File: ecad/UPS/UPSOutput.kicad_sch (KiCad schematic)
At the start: 26 parts, among them J3 USB_C_Receptacle_USB2.0_16P, Q3 IRLR7843TRPBF, U2 MPQ5031GRE-0001-AEC1-P, U3 L78L05_SOT89

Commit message: Moved most components where they belong-ish
Barrel Jack's on the end as well as battery connector for now.  The MOSFET's need to be really close to the caps in the charger module
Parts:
- C10, C11, C12, C60: footprint Capacitor_SMD:C_0805_2012Metric_Pad1.18x1.45mm_HandSolder -> (none)
- C5, C59, C6, C7, C8, C9: footprint Capacitor_SMD:C_0603_1608Metric_Pad1.08x0.95mm_HandSolder -> (none)
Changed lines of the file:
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@@
 			)
 		)
-		(property "Footprint" "Capacitor_SMD:C_0603_1608Metric_Pad1.08x0.95mm_HandSolder"
+		(property "Footprint" ""
 			(at 204.1652 78.74 0)
 			(effects
@@
 			)
 		)
-		(property "Footprint" "Capacitor_SMD:C_0603_1608Metric_Pad1.08x0.95mm_HandSolder"
+		(property "Footprint" ""
 			(at 30.1752 115.57 0)
 			(effects
@@
 			)
 		)
-		(property "Footprint" "Capacitor_SMD:C_0603_1608Metric_Pad1.08x0.95mm_HandSolder"
+		(property "Footprint" ""
 			(at 65.7352 78.74 0)
 			(effects
@@
 			)
 		)
-		(property "Footprint" "Capacitor_SMD:C_0603_1608Metric_Pad1.08x0.95mm_HandSolder"
+		(property "Footprint" ""
 			(at 130.5052 73.66 0)
 			(effects
@@
 			)
 		)
-		(property "Footprint" "Capacitor_SMD:C_0805_2012Metric_Pad1.18x1.45mm_HandSolder"
+		(property "Footprint" ""
 			(at 56.1848 78.74 0)
 			(effects
@@
 			)
 		)
-		(property "Footprint" "Capacitor_SMD:C_0805_2012Metric_Pad1.18x1.45mm_HandSolder"
+		(property "Footprint" ""
 			(at 143.51 81.5848 0)
 			(effects
@@
 			)
 		)
-		(property "Footprint" "Capacitor_SMD:C_0603_1608Metric_Pad1.08x0.95mm_HandSolder"
+		(property "Footprint" ""
 			(at 135.5852 73.66 0)
 			(effects
@@
 			)
 		)
-		(property "Footprint" "Capacitor_SMD:C_0603_1608Metric_Pad1.08x0.95mm_HandSolder"
+		(property "Footprint" ""
 			(at 176.8348 78.74 0)
 			(effects
@@
 			)
 		)
-		(property "Footprint" "Capacitor_SMD:C_0805_2012Metric_Pad1.18x1.45mm_HandSolder"
+		(property "Footprint" ""
 			(at 30.1752 128.27 0)
 			(effects
@@
 			)
 		)
-		(property "Footprint" "Capacitor_SMD:C_0805_2012Metric_Pad1.18x1.45mm_HandSolder"
+		(property "Footprint" ""
 			(at 234.95 84.1248 0)
 			(effects

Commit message: Need to finish some traces, DRC warnings are keeping me from routing to the BQ,
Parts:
- added R35: 68.1k, Resistor_SMD:R_0805_2012Metric_Pad1.20x1.40mm_HandSolder, symbol Device:R
- added SW3: SW_DPDT_x2, UPS:SW_EG1218, symbol Switch:SW_DPDT_x2
- C10, C11, C12, C60: footprint (none) -> Capacitor_SMD:C_0805_2012Metric_Pad1.18x1.45mm_HandSolder
- C5, C59, C6, C7, C8, C9: footprint (none) -> Capacitor_SMD:C_0603_1608Metric_Pad1.08x0.95mm_HandSolder
- R6, R7: footprint (none) -> Resistor_SMD:R_1206_3216Metric_Pad1.30x1.75mm_HandSolder
- R8: footprint (none) -> Resistor_SMD:R_0805_2012Metric_Pad1.20x1.40mm_HandSolder
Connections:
- net GND: now also R35.2
- net D+: now reaches C7.1, D4.1 (K), J3.A6 (D+), J3.B6 (D+), U2.16 (DP)
- net CC1: now reaches D1.1 (K), J3.A5 (CC1), R7.1
- net VBUS_out: now reaches C11.2, C12.1, D5.1 (K), J3.A4 (VBUS), J3.A9 (VBUS), J3.B4 (VBUS), J3.B9 (VBUS), Q3.2 (D), TP6.1, U2.20 (VBUS_P)
- net D-: now reaches C8.1, D3.1 (K), J3.A7 (D-), J3.B7 (D-), U2.17 (DM)
- net CC2: now reaches D2.1 (K), J3.B5 (CC2), R6.2
- net at U2.19 (VDRV): now also SW3.1 (A); no longer Q3.1 (G)
- new net: Q3.1 (G), SW3.2 (B)
- new net: R35.1, SW3.3 (C)
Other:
- moved on the sheet: Q3

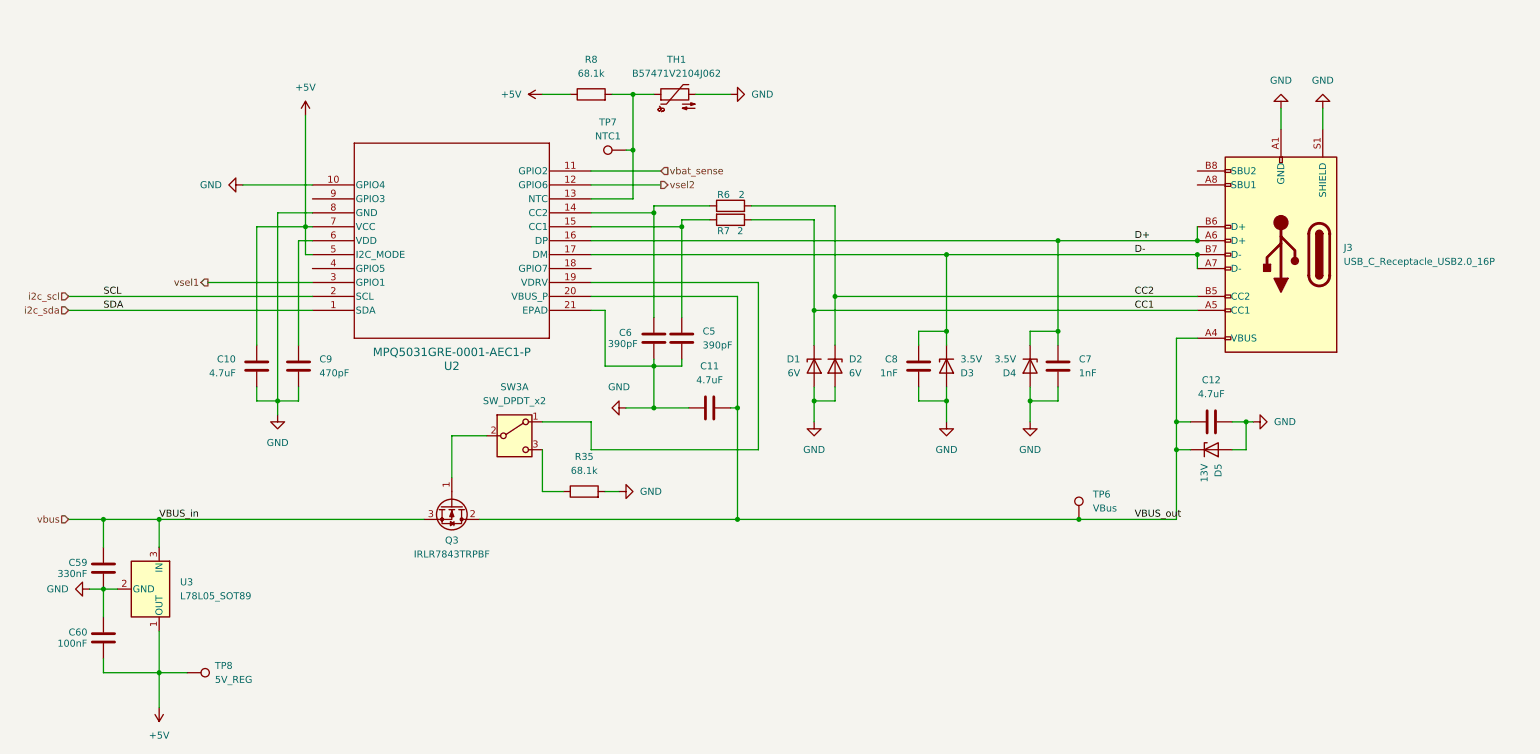
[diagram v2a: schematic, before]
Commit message: Ty's VBATSENSE Changes
Let me know if I messed this part up, did a small amount
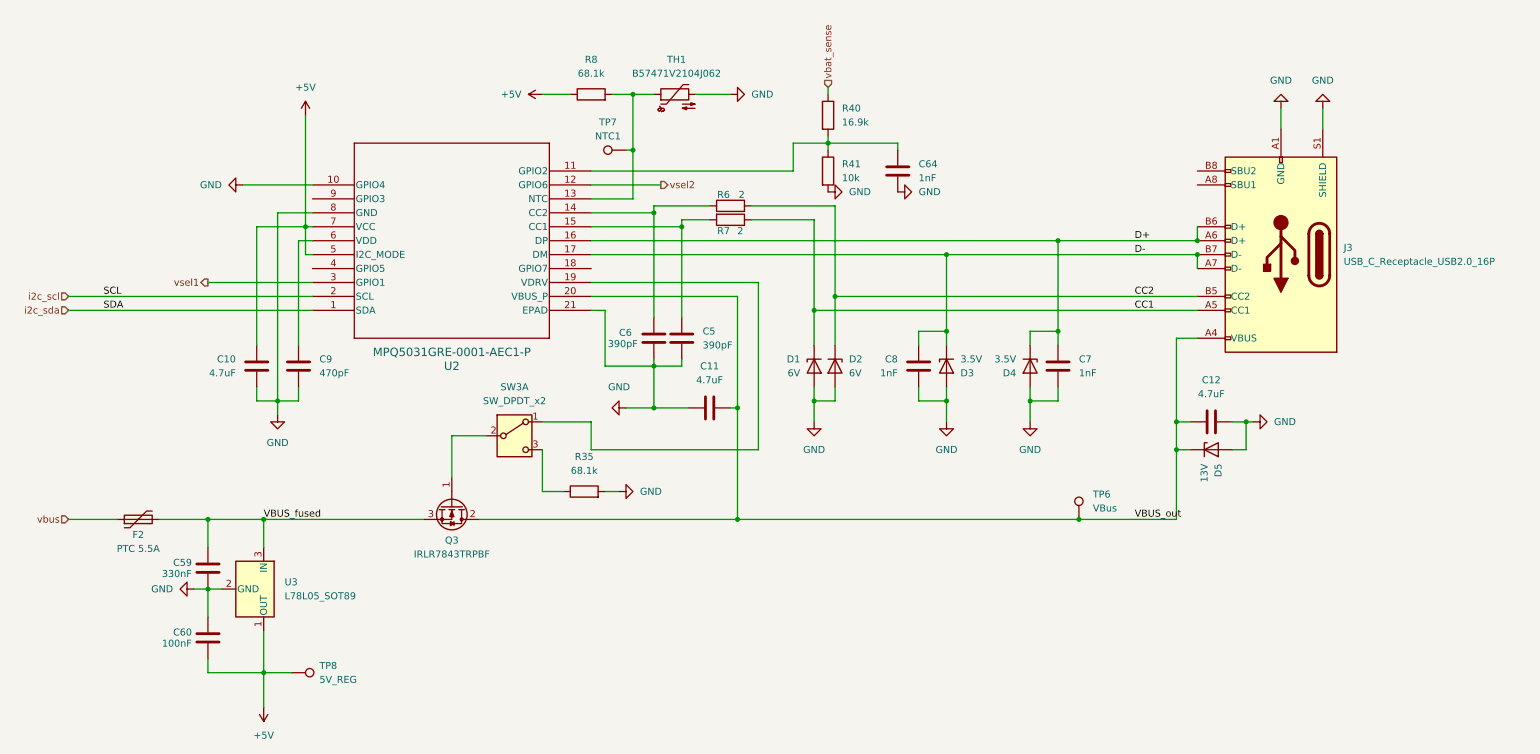
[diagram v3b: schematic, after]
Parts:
- added C64: 1nF, symbol Device:C
- added F2: PTC 5.5A, Fuse:Fuse_1210_3225Metric_Pad1.42x2.65mm_HandSolder, symbol Device:Polyfuse
- added R40: 16.9k, Resistor_SMD:R_0201_0603Metric_Pad0.64x0.40mm_HandSolder, symbol Device:R
- added R41: 10k, Resistor_SMD:R_0201_0603Metric_Pad0.64x0.40mm_HandSolder, symbol Device:R
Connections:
- net GND: now also C64.2, R41.2
- net vbat_sense: now also R40.1; no longer U2.11 (GPIO2)
- net vbus: now also F2.1; no longer C59.1, Q3.3 (S), U3.3 (IN)
- new net: C64.1, R40.2, R41.1, U2.11 (GPIO2)
- new net VBUS_fused: C59.1, F2.2, Q3.3 (S), U3.3 (IN)
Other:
- moved on the sheet: C59, C60, TP8, U3

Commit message: DRC is angry but everything has a route
Angry about a lot of the vias in the top right specifically, there's A LOT of issues with clearance I want to look at, taking another break for now.
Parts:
- C64: footprint (none) -> Capacitor_SMD:C_0201_0603Metric
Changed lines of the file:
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@@
 			)
 		)
-		(property "Footprint" ""
+		(property "Footprint" "Capacitor_SMD:C_0201_0603Metric"
 			(at 174.9552 43.18 0)
 			(effects
